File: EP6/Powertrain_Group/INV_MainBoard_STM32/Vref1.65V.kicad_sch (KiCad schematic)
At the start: 6 parts, among them U1 OPA340NA

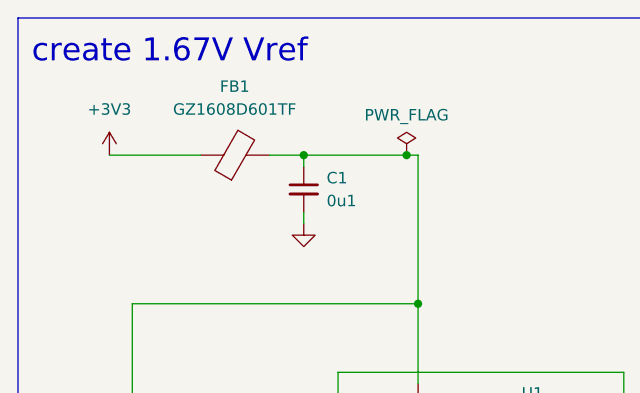
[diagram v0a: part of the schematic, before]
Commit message: batch update for JLCPCB 241117
6SBMS
ACC_HVLV1
INV_CurrentSense2
INV_CurrentSense3
DClinkCap1
INV_MainBoard_STM32
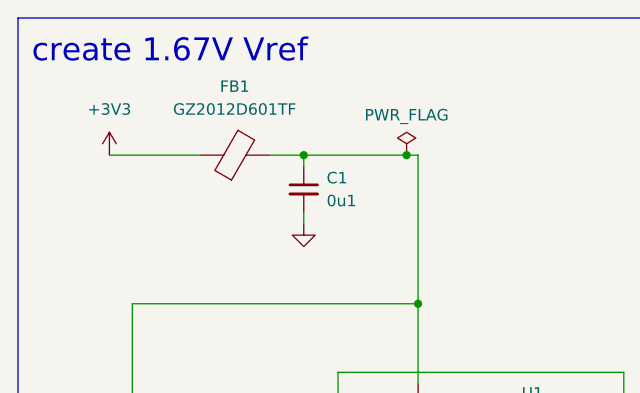
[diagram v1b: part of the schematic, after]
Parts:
- FB1: value GZ1608D601TF -> GZ2012D601TF
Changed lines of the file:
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@@
 	(title_block
 		(title "INV_MainBoard")
-		(date "2024-11-15")
-		(rev "1")
+		(date "2024-11-16")
+		(rev "1.0")
 		(company "NTURacing Team")
 		(comment 1 "郭哲明 Jack Kuo")
@@
 			)
 		)
-		(property "Value" "GZ1608D601TF"
+		(property "Value" "GZ2012D601TF"
 			(at 52.0192 31.75 90)
 			(effects

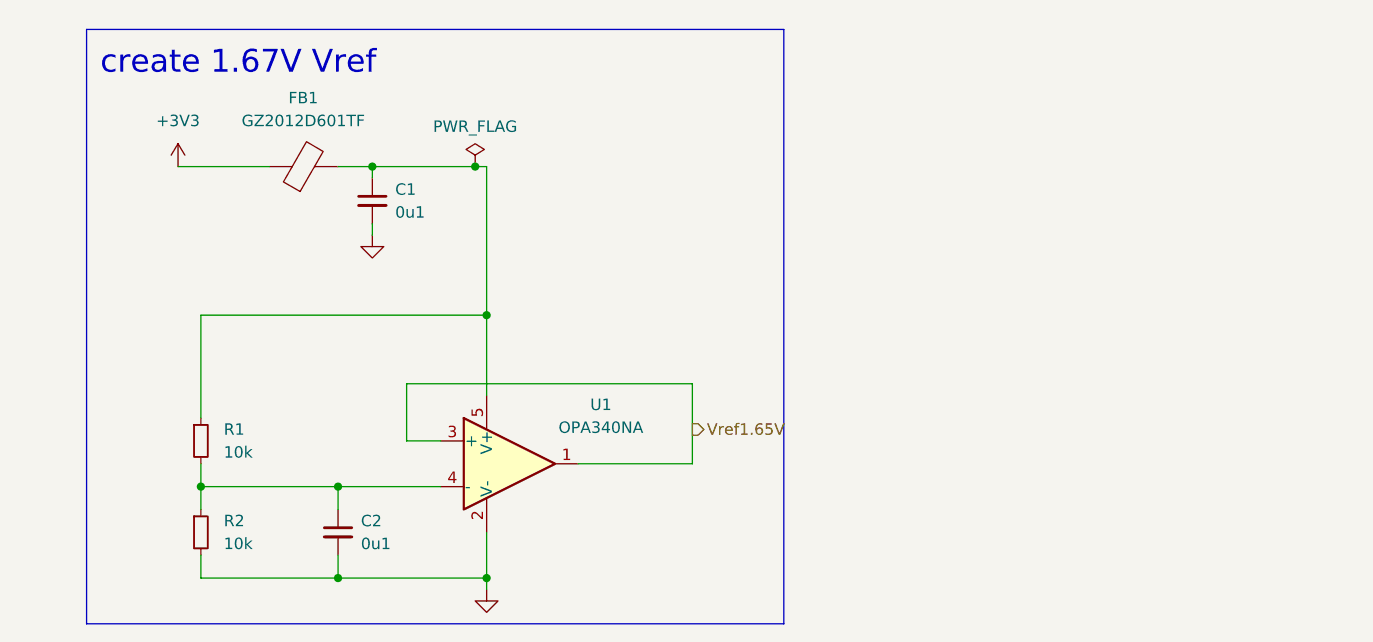
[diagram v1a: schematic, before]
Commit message: update INV_MainBoard_STM32 to V2.0
big update to match new INV_GateDriver
and use H743ZI as MCU
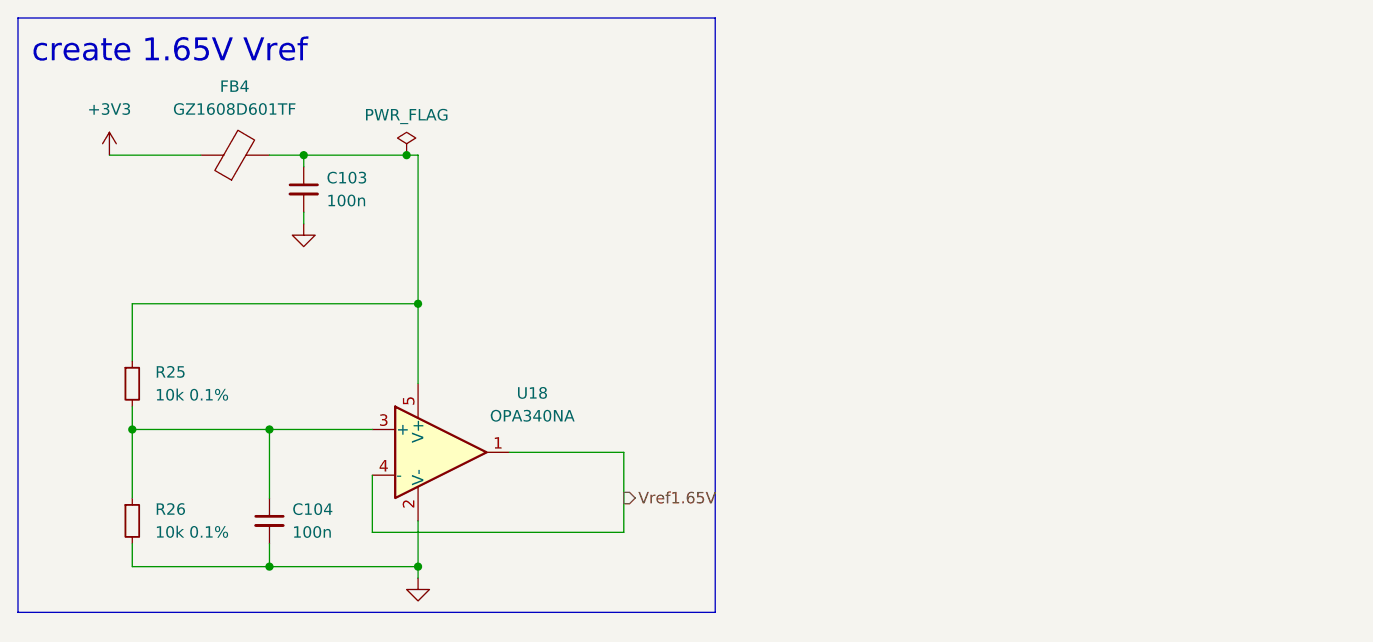
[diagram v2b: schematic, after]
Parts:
- removed C1, C2: 0u1, Capacitor_SMD:C_0402_1005Metric, symbol Device:C_Small
- removed FB1: GZ2012D601TF, Inductor_SMD:L_0805_2012Metric, symbol Device:FerriteBead
- removed R1, R2: 10k, Resistor_SMD:R_0402_1005Metric, symbol Device:R_Small
- removed U1: OPA340NA, Package_TO_SOT_SMD:SOT-23-5, symbol Amplifier_Operational:OPA340NA
- added C103, C104: 100n, Capacitor_SMD:C_0402_1005Metric, symbol Device:C_Small
- added FB4: GZ1608D601TF, Capacitor_SMD:C_0603_1608Metric, symbol Device:FerriteBead
- added R25, R26: 10k 0.1%, Resistor_SMD:R_0402_1005Metric, symbol Device:R_Small
- added U18: OPA340NA, Package_TO_SOT_SMD:SOT-23-5, symbol Amplifier_Operational:OPA340NA
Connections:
- net +3V3: now also FB4.1
- net GND: now also C103.2, C104.2, R26.2, U18.2 (V-)
- net Vref1.65V: now also U18.1, U18.4 (-)
- new net: C104.1, R25.2, R26.1, U18.3 (+)
- new net: C103.1, FB4.2, R25.1, U18.5 (V+)
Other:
- note added: "create 1.65V Vref"
- note removed: "create 1.67V Vref"
- title: INV_MainBoard -> INV_MainBoard_STM32

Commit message: update INV_MainBoard_STM32 to V2.1
update for JLCPCB, include change in 1.65 Vref and some name change for easier JLCPCBA BOM selection
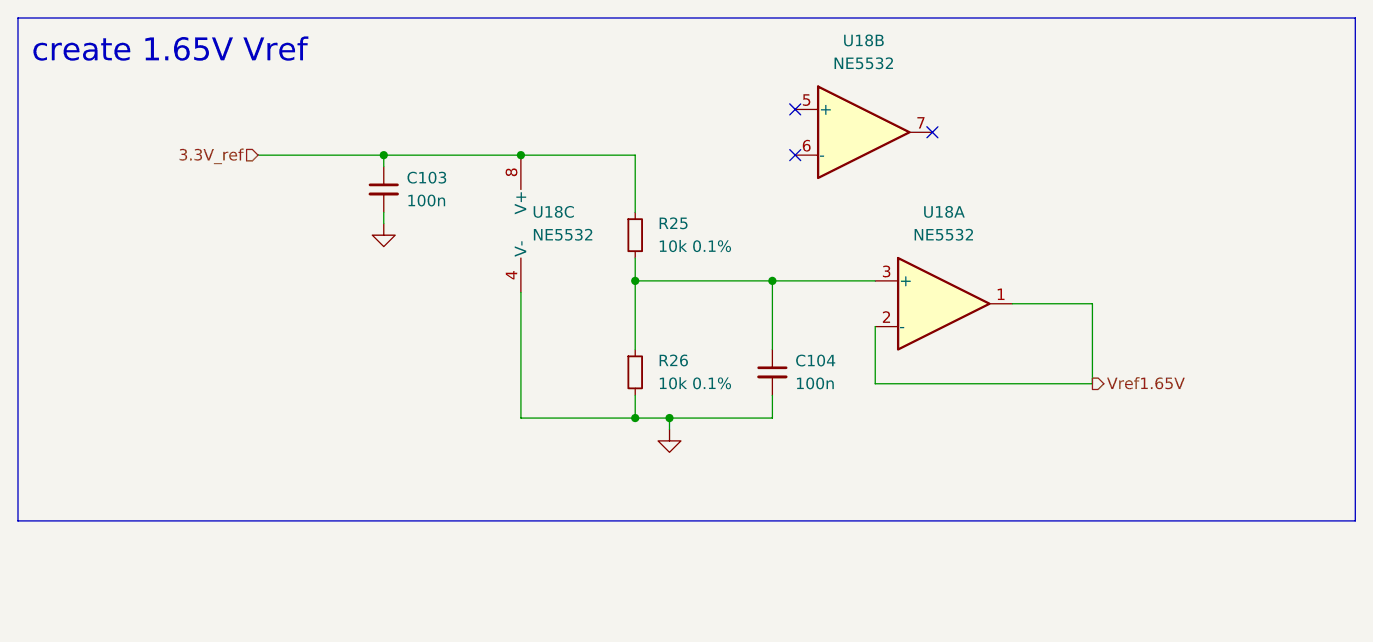
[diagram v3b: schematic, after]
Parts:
- removed FB4: GZ1608D601TF, Capacitor_SMD:C_0603_1608Metric, symbol Device:FerriteBead
- removed U18: OPA340NA, Package_TO_SOT_SMD:SOT-23-5, symbol Amplifier_Operational:OPA340NA
- added U18: NE5532, Package_SO:SOIC-8_3.9x4.9mm_P1.27mm, symbol Amplifier_Operational:NE5532
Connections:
- net GND: now also U18.4 (V-)
- net Vref1.65V: now also U18.1, U18.2 (-)
- net at C104.1, R25.2, R26.1: now also U18.3 (+)
- net 3.3V_ref: now reaches C103.1, R25.1
- net 3.3V_ref: now also U18.8 (V+)
- no-connect marks 0 -> 3
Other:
- moved on the sheet: C103, C104, R25, R26

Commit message: update INV_MainBoard_STM32 to V3.0
PCB: INV_MainBoard_STM32 V3.0
V3.0 remove low volte trig
     add RC filt for OCP, OTP
     dedicated OTP, OCP pull down gate enable
     pending: fault hardware OTP/OCP latch
     pending: add QSPI DRAM
     use JST PH
     exterinal pull up for flt, ready
     fix CAN1, 2 label on board
     use 1k, 2k for encoder divider
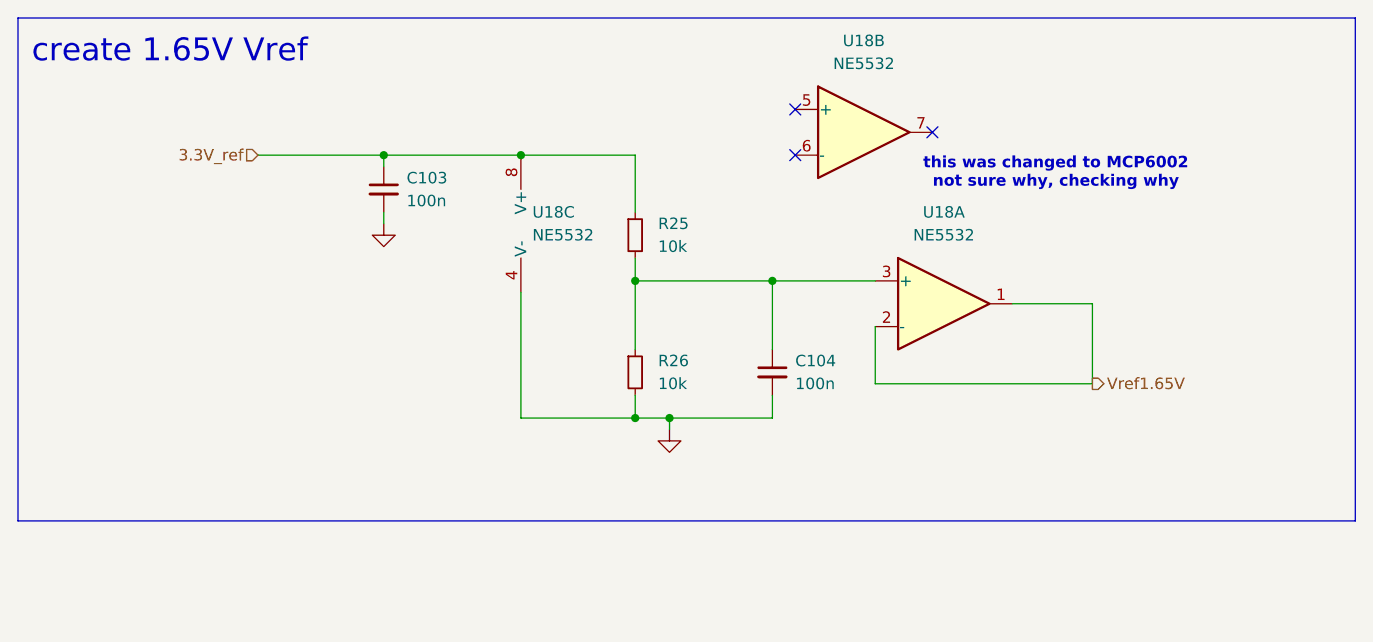
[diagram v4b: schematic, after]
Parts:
- R25, R26: value 10k 0.1% -> 10k
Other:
- note added: "this was changed to MCP6002 not sure why, checking why"
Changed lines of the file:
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@@
 	(title_block
 		(title "INV_MainBoard_STM32")
-		(date "2025-02-28")
-		(rev "2.1")
+		(date "2025-06-29")
+		(rev "3.0")
 		(company "NTURacing Team")
 		(comment 1 "郭哲明 Jack Kuo")
@@
 		(fill
 			(type none)
+		)
+	)
+	(text "this was changed to MCP6002\nnot sure why, checking why"
+		(exclude_from_sim no)
+		(at 135.636 37.592 0)
+		(effects
+			(font
+				(size 1.27 1.27)
+				(thickness 0.254)
+				(bold yes)
+				(color 255 0 0 1)
+			)
 		)
 	)
@@
 		(fields_autoplaced yes)
 		(property "Reference" "R26"
-			(at 91.44 58.42 0)
+			(at 91.44 58.4199 0)
 			(effects
 				(font
@@
 			)
 		)
-		(property "Value" "10k 0.1%"
-			(at 91.44 60.96 0)
+		(property "Value" "10k"
+			(at 91.44 60.9599 0)
 			(effects
 				(font
@@
 		(fields_autoplaced yes)
 		(property "Reference" "R25"
-			(at 91.44 43.18 0)
+			(at 91.44 43.1799 0)
 			(effects
 				(font
@@
 			)
 		)
-		(property "Value" "10k 0.1%"
-			(at 91.44 45.72 0)
-			(effects
-				(font
+		(property "Value" "10k"
+			(at 91.44 45.7199 0)
+			(effects
+				(font
